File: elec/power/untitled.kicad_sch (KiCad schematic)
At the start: 46 parts, among them J1 Screw_Terminal_01x05, J2 Conn_01x03, J3 Conn_01x02, J4 Conn_01x04, Q1 DISCHARGE_FET, Q2 CHARGE_FET, U1 BQ7791501PWR

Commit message: Pretty much what I can do until this point
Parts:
- added D1, D2, D3, D4, D5: RED, symbol Device:LED
- added R10, R11, R12, R13, R14: 1k, Resistor_SMD:R_0402_1005Metric, symbol Device:R
- added TP2: AVDD, TestPoint:TestPoint_Pad_D2.0mm, symbol Connector:TestPoint
- added TP3: VDD, TestPoint:TestPoint_Pad_D2.0mm, symbol Connector:TestPoint
- TP5: renamed from TP3; value V_TS -> VTS
- renumbered D1 to D6, D2 to D7, D4 to D8, R10 to R15, R11 to R16, R12 to R17, R13 to R18, R15 to R19, R14 to R20, R16 to R21, R17 to R22, R18 to R23, TP2 to TP4, TP4 to TP6, TP5 to TP7
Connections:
- net AVDD: now also TP2.1
- net BATT_P: now also D5.2 (A)
- net C1: now also D2.2 (A)
- net C2: now also D3.2 (A)
- net C3: now also D4.2 (A)
- net GND: now also D1.2 (A)
- net VC0: now also R10.2
- net VC1: now also R11.2
- net VC2: now also R12.2
- net VC3: now also R13.2
- net VC4: now also R14.2
- net VDD: now also TP3.1
- new net: D3.1 (K), R12.1
- new net: D4.1 (K), R13.1
- new net: D2.1 (K), R11.1
- new net: D1.1 (K), R10.1
- new net: D5.1 (K), R14.1
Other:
- note removed: "RC filter to improve current sensing"
- moved on the sheet: C10, C11, C12, C6, C7, C8, C9, D6, D7, D8, J3, Q1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

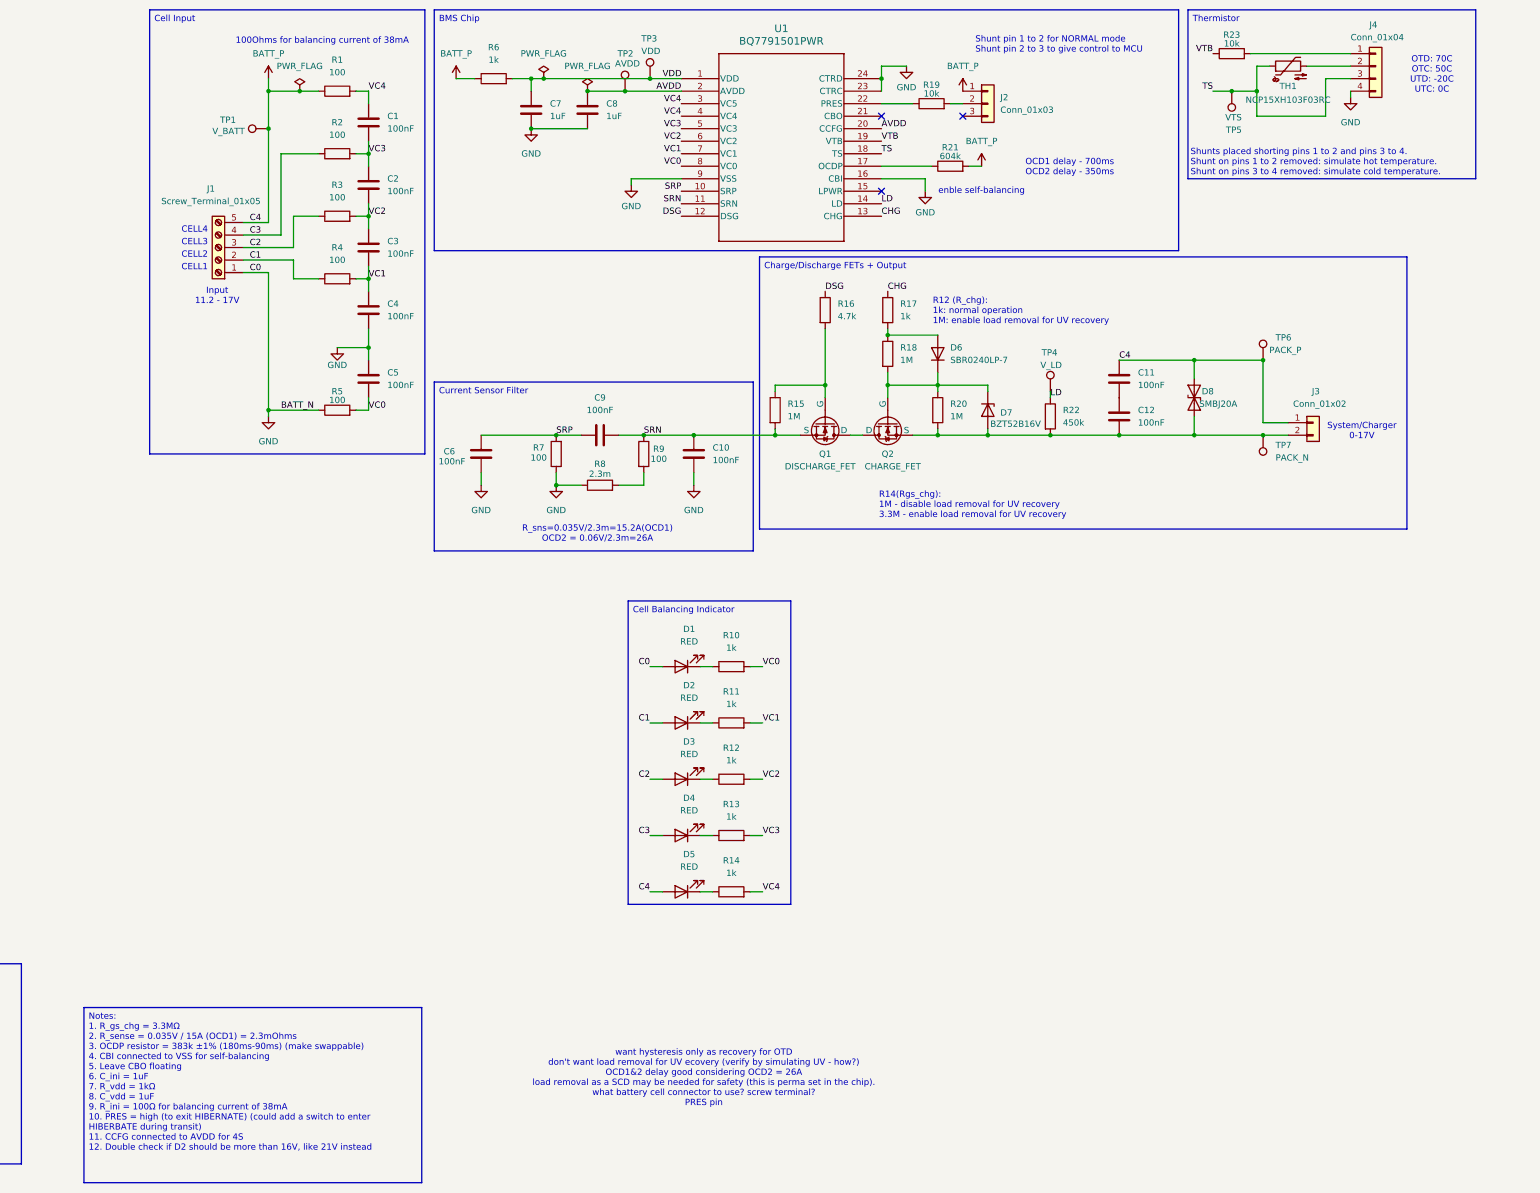
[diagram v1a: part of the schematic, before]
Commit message: Add fuel gauge schematic
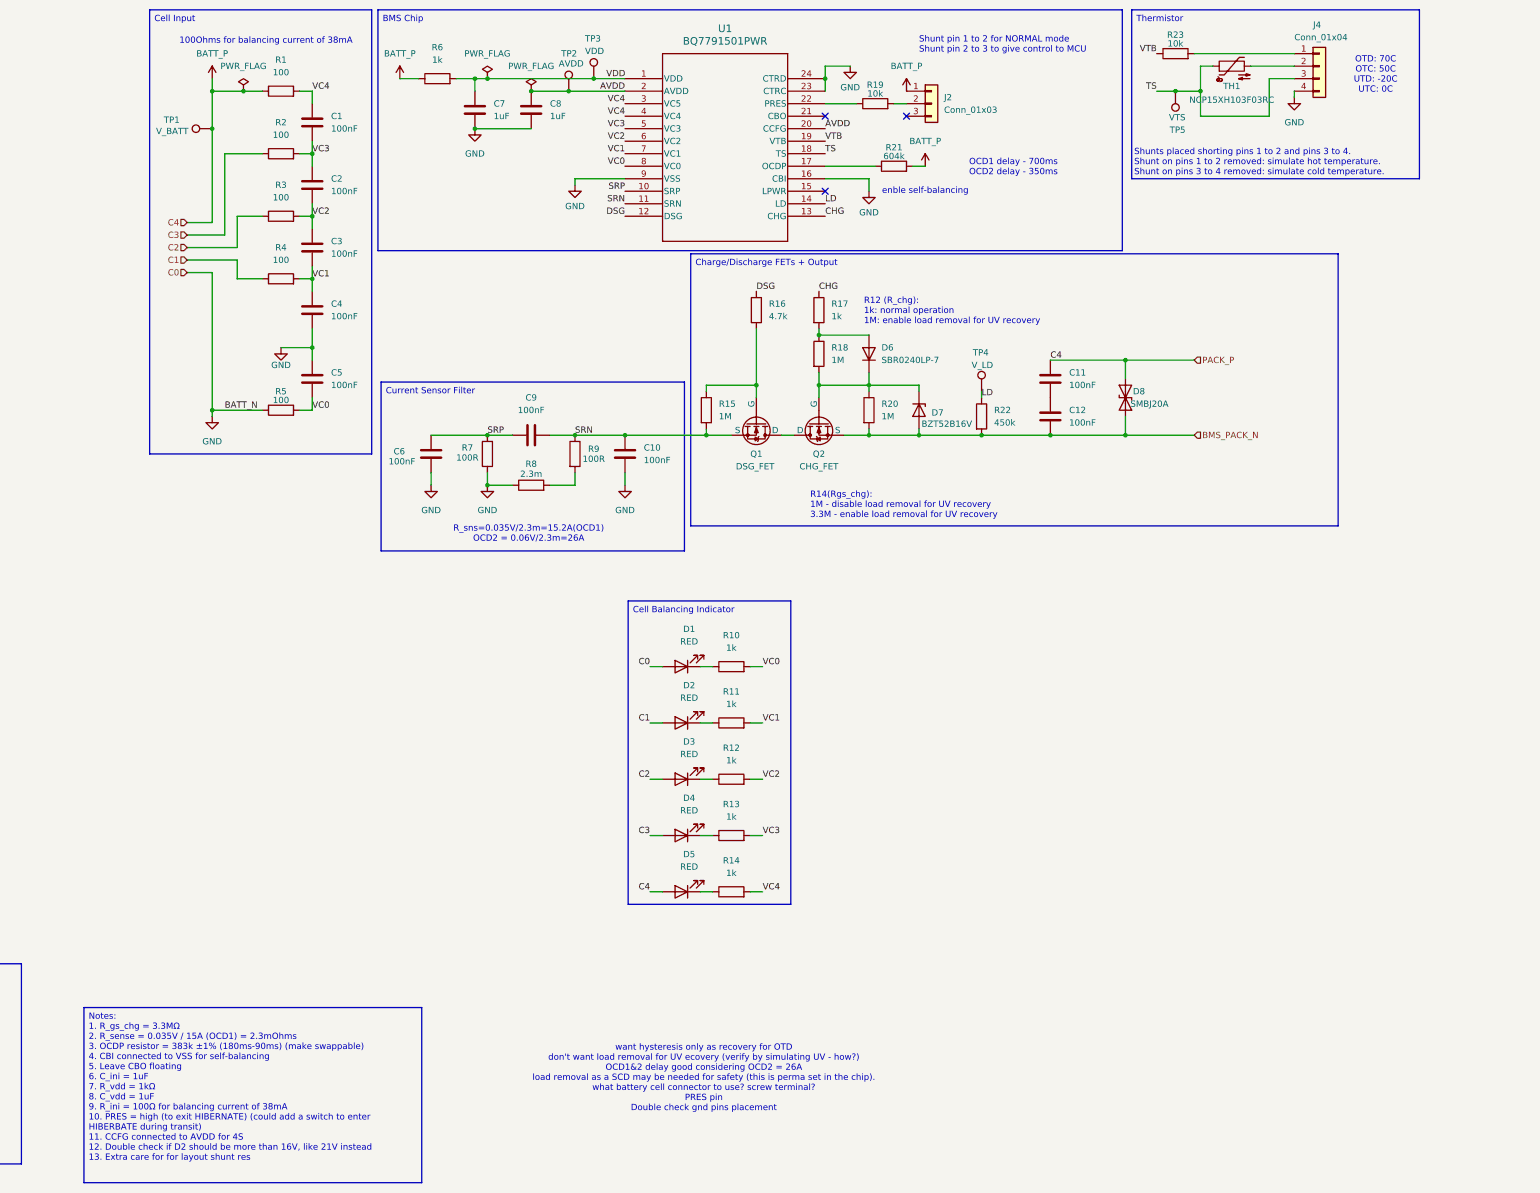
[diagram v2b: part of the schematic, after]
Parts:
- removed J1: Screw_Terminal_01x05, symbol Connector:Screw_Terminal_01x05
- removed J3: Conn_01x02, symbol Connector_Generic:Conn_01x02
- removed TP6: PACK_P, TestPoint:TestPoint_Pad_D2.0mm, symbol Connector:TestPoint
- removed TP7: PACK_N, TestPoint:TestPoint_Pad_D2.0mm, symbol Connector:TestPoint
- Q1: value DISCHARGE_FET -> DSG_FET
- Q2: value CHARGE_FET -> CHG_FET
- R7, R9: value 100 -> 100R
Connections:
- net BMS_PACK_N: now reaches C12.2, D7.2 (A), D8.1 (A1), Q2.3 (S), R20.2, R22.2
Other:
- note added: "want hysteresis only as recovery for OTD don't want load removal for UV ecovery (verify by simulating UV - how?) OCD1&2 delay good considering OCD2 = 26A load removal as a SCD may be needed for safety (this is perma set in the chip). what battery cell connector to use? screw terminal? PRES pin Double check gnd pins placement"
- note removed: "CELL1"
- note removed: "CELL2"
- note removed: "CELL3"
- note removed: "CELL4"
- note removed: "Input 11.2 - 17V"
- note removed: "System/Charger 0-17V"
- note removed: "want hysteresis only as recovery for OTD don't want load removal for UV ecovery (verify by simulating UV - how?) OCD1&2 delay good considering OCD2 = 26A load removal as a SCD may be needed for safety (this is perma set in the chip). what battery cell connector to use? screw terminal? PRES pin"
- moved on the sheet: C1, C10, C11, C12, C2, C3, C4, C5, C6, C7, C8, C9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
